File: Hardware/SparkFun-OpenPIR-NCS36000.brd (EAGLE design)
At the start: 27.9 x 35.6 mm, 39 parts, among them U1 NCS36000, U2 PIR

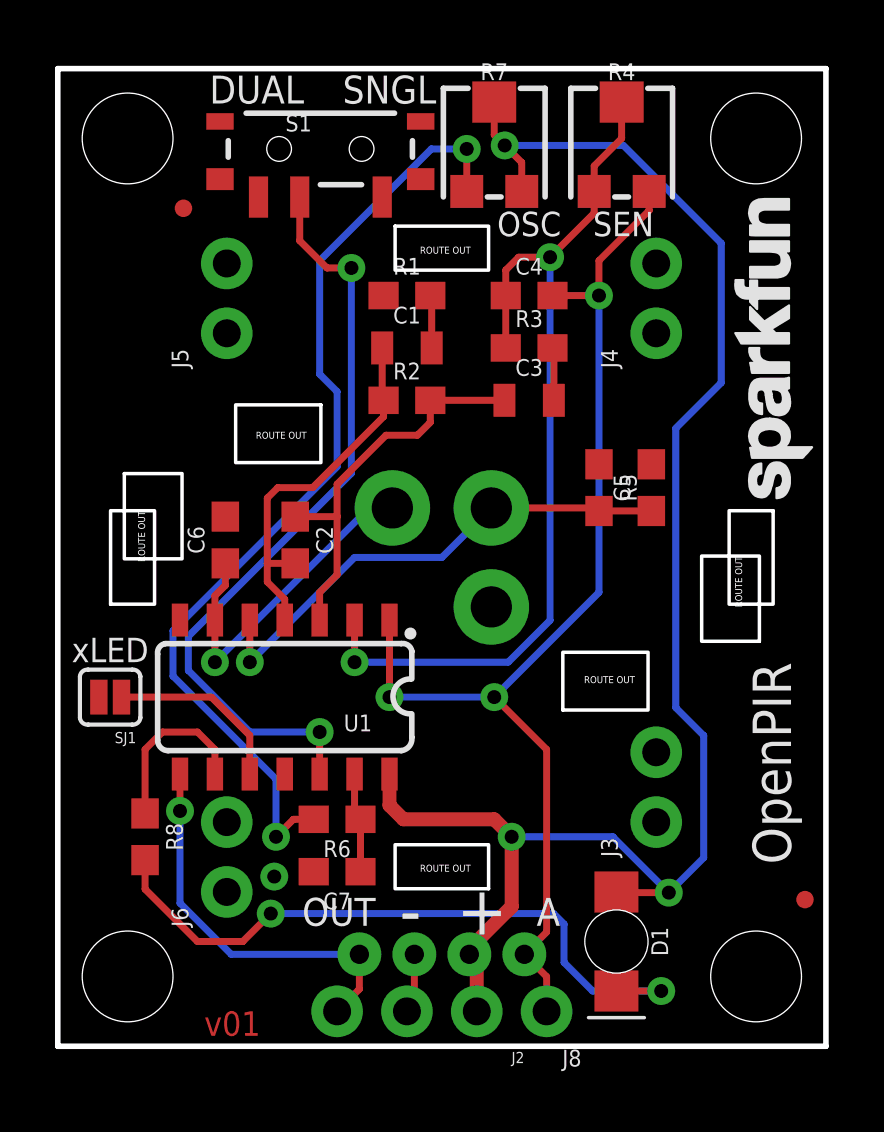
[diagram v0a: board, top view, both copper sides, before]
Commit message: Remove a few lenses, re-wire pot, re-routing
- Removed ZAA09GIT1 lens & PTH holes that would hold it in. (Would be mounted at incorrect curve/distance.)
- Removed ZNCL11 lens. Low stock, uncommon footprint.
- Re-wired sensitivity pot so "turning it up" increases sensitivity.
- Re-routing now that there are fewer mill-outs and holes.
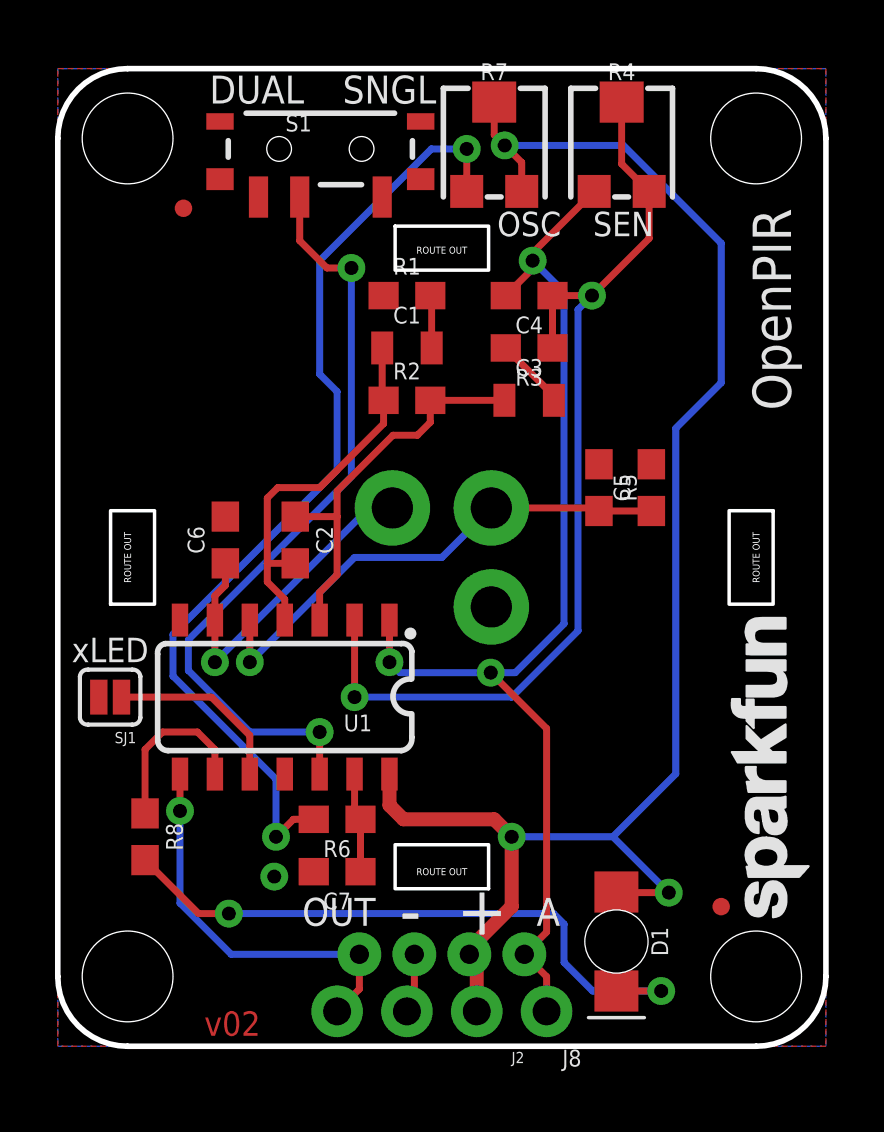
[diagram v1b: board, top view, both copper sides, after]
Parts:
- removed J3, J4, J5, J6: (no value), SparkFun-Connectors:1X02_NO_SILK
- removed U$2: AA 0.9 GI T1, openPIR-temp:LENS-AA-0.9-GI-T1
- removed U$3: NCL-11, openPIR-temp:LENS-NCL-11
- moved LOGO1 15.2 mm to (27.8, 4.19)
- moved FD2 3.06 mm to (24.1, 5.08)
- turned C4 to 180 degrees
- turned R3 to 180 degrees
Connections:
- net A_OUT: now also R4.1; no longer R4.3
- net N$7: now also R4.3; no longer R4.1
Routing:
- net N$7: track 33.8 -> 36.0 mm
- net VCC: track 59.9 -> 57.9 mm
- net N$9: track 24.7 -> 23.2 mm
- net N$4: track 1.93 -> 2.63 mm
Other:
- outline, holes or cut-outs redrawn
- board text added: "v02"
- board text removed: "v01"

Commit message: Moving xLED jumper to more accessible location
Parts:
- moved SJ1 12.7 mm to (2.54, 25.4), turned to 0 degrees
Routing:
- net !LED_EN!: track 6.65 -> 20.2 mm
- net GND: vias 1 -> 3
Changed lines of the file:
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@@
 <text x="10.0965" y="4.3815" size="1.016" layer="22" font="vector" ratio="15" rot="MR0" align="bottom-center">OUT</text>
 <text x="15.1765" y="4.064" size="1.778" layer="22" font="vector" ratio="15" rot="MR0" align="bottom-center">+</text>
-<text x="1.905" y="13.97" size="0.889" layer="21" font="vector" ratio="15" align="bottom-center">xLED</text>
+<text x="2.54" y="26.67" size="0.889" layer="21" font="vector" ratio="15" align="bottom-center">xLED</text>
 <dimension x1="0" y1="0" x2="2.54" y2="2.54" x3="1.27" y3="-1.27" textsize="0.889" textratio="15" layer="47" dtype="horizontal" width="0.127" unit="inch" precision="3"/>
 <dimension x1="0" y1="0" x2="25.4" y2="2.54" x3="12.7" y3="-6.35" textsize="0.889" textratio="15" layer="47" dtype="horizontal" width="0.127" unit="inch" precision="3"/>
@@
 <attribute name="PROD_ID" value="RES-07856" x="3.175" y="7.62" size="1.778" layer="27" ratio="15" rot="R270" display="off"/>
 </element>
-<element name="SJ1" library="SparkFun-Retired" package="SJ_2S" value="LED-EN" x="1.905" y="12.7" rot="R180"/>
+<element name="SJ1" library="SparkFun-Retired" package="SJ_2S" value="LED-EN" x="2.54" y="25.4"/>
 <element name="S1" library="SparkFun-Electromechanical" package="SWITCH-SPST-SMD-A" value="" x="9.5504" y="32.639">
 <attribute name="PROD_ID" value="SWCH-10651" x="9.5504" y="32.639" size="1.778" layer="27" ratio="15" display="off"/>
@@
 <wire x1="12.7" y1="1.27" x2="12.97" y2="1.54" width="0.254" layer="1"/>
 <wire x1="12.97" y1="1.54" x2="12.97" y2="3.344" width="0.254" layer="1"/>
+<via x="4.445" y="17.0942" extent="1-16" drill="0.508"/>
+<via x="7.62" y="12.6492" extent="1-16" drill="0.508"/>
 </signal>
 <signal name="N$2">
@@
 <contactref element="U1" pad="10"/>
 <contactref element="SJ1" pad="1"/>
-<wire x1="2.3169" y1="12.7" x2="5.588" y2="12.7" width="0.254" layer="1"/>
-<wire x1="5.588" y1="12.7" x2="6.985" y2="11.303" width="0.254" layer="1"/>
-<wire x1="6.985" y1="9.9" x2="6.985" y2="11.303" width="0.254" layer="1"/>
+<wire x1="5.588" y1="12.192" x2="6.985" y2="10.795" width="0.254" layer="1"/>
+<wire x1="6.985" y1="9.9" x2="6.985" y2="10.795" width="0.254" layer="1"/>
+<wire x1="2.1281" y1="25.4" x2="2.1281" y2="23.7181" width="0.254" layer="1"/>
+<wire x1="5.588" y1="12.192" x2="2.921" y2="12.192" width="0.254" layer="1"/>
+<wire x1="2.921" y1="12.192" x2="0.762" y2="14.351" width="0.254" layer="1"/>
+<wire x1="0.762" y1="14.351" x2="0.762" y2="22.352" width="0.254" layer="1"/>
+<wire x1="0.762" y1="22.352" x2="2.1281" y2="23.7181" width="0.254" layer="1"/>
 </signal>
 <signal name="LED">
